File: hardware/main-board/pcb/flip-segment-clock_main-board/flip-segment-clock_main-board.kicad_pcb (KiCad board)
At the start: 2 copper layers, 29.4 x 23 mm, 59 parts, among them IC1 STM32G071CBT6, IC10 A3909GLNTR-T, IC11 A3909GLNTR-T, IC12 A3909GLNTR-T, IC13 A3909GLNTR-T, IC14 A3909GLNTR-T, IC15 A3909GLNTR-T, IC16 A3909GLNTR-T, IC17 A3909GLNTR-T, IC18 A3909GLNTR-T, IC19 A3909GLNTR-T, IC2 DS3231MZ+TRL, IC3 TPS62177DQCR, IC4 A3909GLNTR-T, IC5 A3909GLNTR-T, IC6 A3909GLNTR-T, IC7 A3909GLNTR-T, IC8 A3909GLNTR-T, IC9 A3909GLNTR-T, J1 Barrel_Jack, J3 Digit 1, J4 Digit 2, J5 Digit 3, J6 Digit 4, U1 74HC595, U2 74HC595

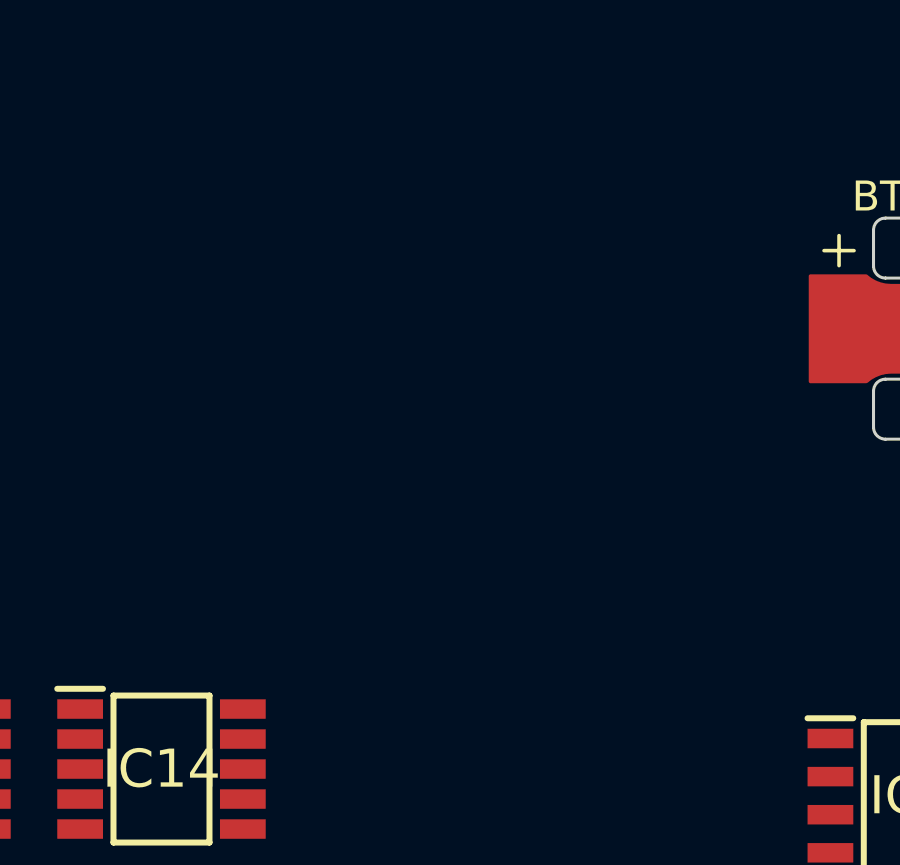
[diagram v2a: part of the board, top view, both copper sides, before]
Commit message: Changelog/design notes for Segment Drivers
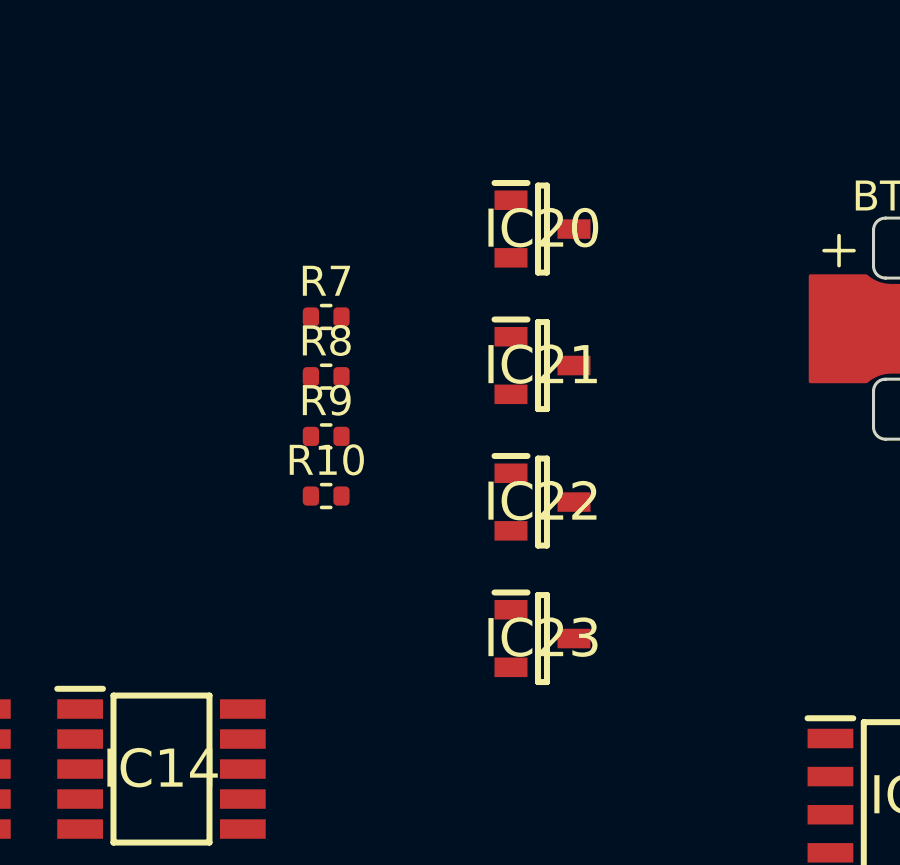
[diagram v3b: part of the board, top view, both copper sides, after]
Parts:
- added IC20: DMN6075S-7, SamacSys_Parts:SOT96P240X110-3N, F.Cu at (97.7, 60.6)
- added IC21: DMN6075S-7, SamacSys_Parts:SOT96P240X110-3N, F.Cu at (97.7, 65.2)
- added IC22: DMN6075S-7, SamacSys_Parts:SOT96P240X110-3N, F.Cu at (97.7, 69.7)
- added IC23: DMN6075S-7, SamacSys_Parts:SOT96P240X110-3N, F.Cu at (97.7, 74.2)
- added R10: 100K, Resistor_SMD:R_0402_1005Metric, F.Cu at (90.5, 69.5)
- added R7: 100K, Resistor_SMD:R_0402_1005Metric, F.Cu at (90.5, 63.5)
- added R8: 100K, Resistor_SMD:R_0402_1005Metric, F.Cu at (90.5, 65.5)
- added R9: 100K, Resistor_SMD:R_0402_1005Metric, F.Cu at (90.5, 67.5)
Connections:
- C15 pad 2: DIG1 -> VBB
- C16 pad 2: DIG1 -> VBB
- C17 pad 2: DIG1 -> VBB
- C18 pad 2: DIG2 -> VBB
- C19 pad 2: DIG2 -> VBB
- C20 pad 2: DIG2 -> VBB
- C21 pad 2: DIG2 -> VBB
- C22 pad 2: DIG3 -> VBB
- C23 pad 2: DIG3 -> VBB
- C24 pad 2: DIG3 -> VBB
- C25 pad 2: DIG4 -> VBB
- C26 pad 2: DIG4 -> VBB
- C27 pad 2: DIG4 -> VBB
- C28 pad 2: DIG4 -> VBB
- C3 pad 2: DIG1 -> VBB
- C4 pad 2: DIG3 -> VBB
- IC10 pad 3: DIG2 -> VBB
- IC10 pad 8: GND -> DIG2
- IC11 pad 3: DIG3 -> VBB
- IC11 pad 8: GND -> DIG3
- IC12 pad 3: DIG3 -> VBB
- IC12 pad 8: GND -> DIG3
- IC13 pad 3: DIG3 -> VBB
- IC13 pad 8: GND -> DIG3
- IC14 pad 3: DIG4 -> VBB
- IC14 pad 8: GND -> DIG4
- IC15 pad 3: DIG4 -> VBB
- IC15 pad 8: GND -> DIG4
- IC16 pad 3: DIG4 -> VBB
- IC16 pad 8: GND -> DIG4
- IC17 pad 3: DIG4 -> VBB
- IC17 pad 8: GND -> DIG4
- IC18 pad 3: DIG1 -> VBB
- IC18 pad 8: GND -> DIG1
- IC19 pad 3: DIG3 -> VBB
- IC19 pad 8: GND -> DIG3
- IC4 pad 3: DIG1 -> VBB
- IC4 pad 8: GND -> DIG1
- IC5 pad 3: DIG1 -> VBB
- IC5 pad 8: GND -> DIG1
- IC6 pad 3: DIG1 -> VBB
- IC6 pad 8: GND -> DIG1
- IC7 pad 3: DIG2 -> VBB
- IC7 pad 8: GND -> DIG2
- IC8 pad 3: DIG2 -> VBB
- IC8 pad 8: GND -> DIG2
- IC9 pad 3: DIG2 -> VBB
- IC9 pad 8: GND -> DIG2
